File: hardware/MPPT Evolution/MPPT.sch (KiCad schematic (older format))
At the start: 92 parts, among them P1 CONN_01X02, P2 CONN_01X05, P3 CONN_01X02, P4 CONN_01X02, P5 CONN_01X02, P6 CONN_01X02, P7 CONN_01X02, U1 LTC3129, U2 LTC3129, U3 LTC3129, U4 LTC3129, U5 LTC3129, U6 ZXCT1009, U7 ZXCT1009

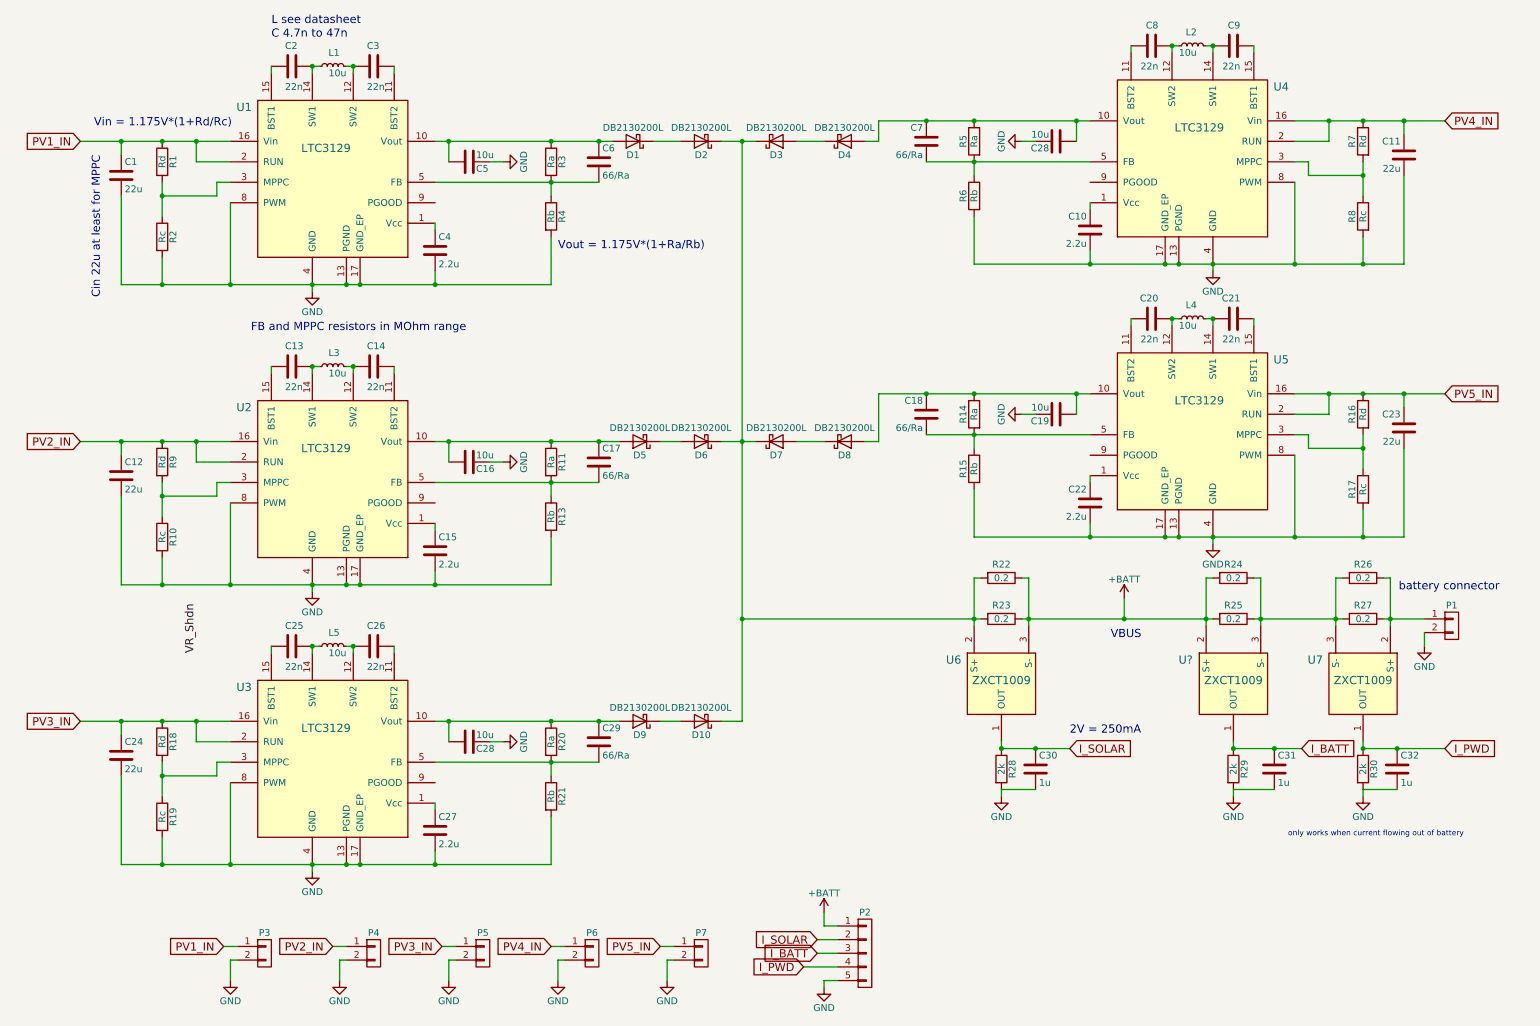
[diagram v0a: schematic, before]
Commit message: Added out pins from panels to MCU
Added out pins from panels to MCU so voltage of each one can be measured
by CPU
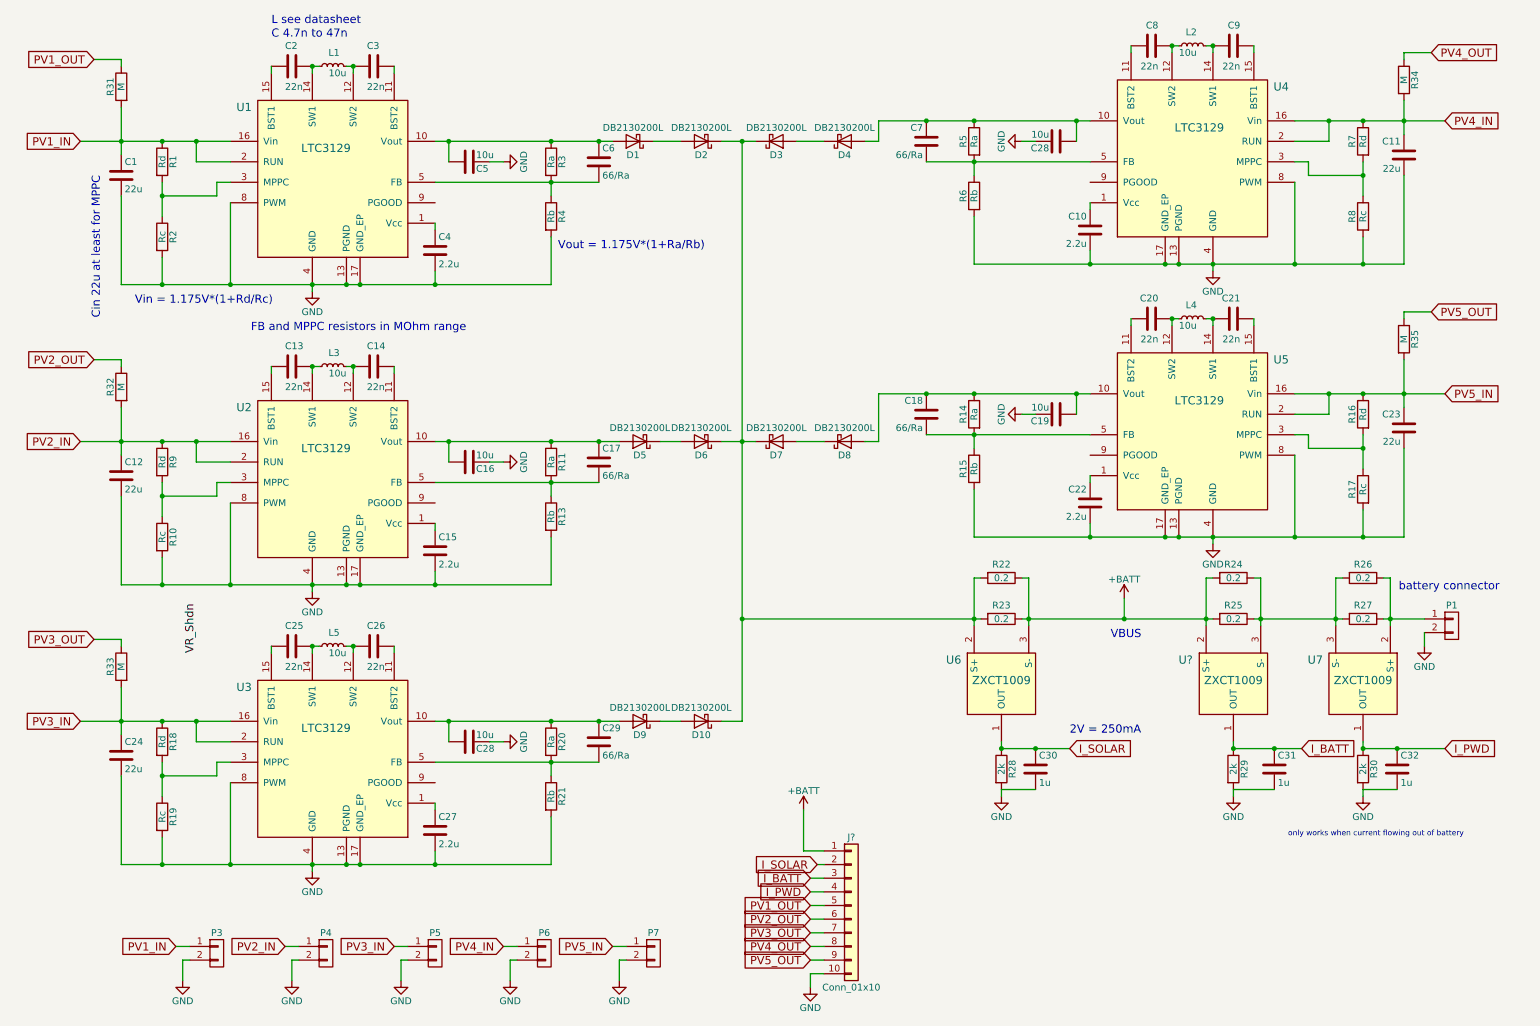
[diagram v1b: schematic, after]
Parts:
- removed P2: CONN_01X05, Pin_Headers:Pin_Header_Straight_1x05, symbol CONN_01X05
- added J?: Conn_01x10, symbol Conn_01x10
- added R31, R32, R33, R34, R35: M, Resistors_SMD:R_0603, symbol R
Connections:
- net +BATT: now also J?.1 (Pin_1)
- net GND: now also J?.10 (Pin_10)
- net I_BATT: now also J?.3 (Pin_3)
- net I_PWD: now also J?.4 (Pin_4)
- net I_SOLAR: now also J?.2 (Pin_2)
- net PV1_IN: now also R31.2
- net PV2_IN: now also R32.2
- net PV3_IN: now also R33.2
- net PV4_IN: now also R34.2
- net PV5_IN: now also R35.2
- new net PV1_OUT: J?.5 (Pin_5), R31.1
- new net PV2_OUT: J?.6 (Pin_6), R32.1
- new net PV3_OUT: J?.7 (Pin_7), R33.1
- new net PV4_OUT: J?.8 (Pin_8), R34.1
- new net PV5_OUT: J?.9 (Pin_9), R35.1
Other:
- moved on the sheet: P3, P4, P5, P6, P7

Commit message: MPPT evolution added missing models, replaced componentes
MPPT evolution added missing models, replaced componentes, routed again.
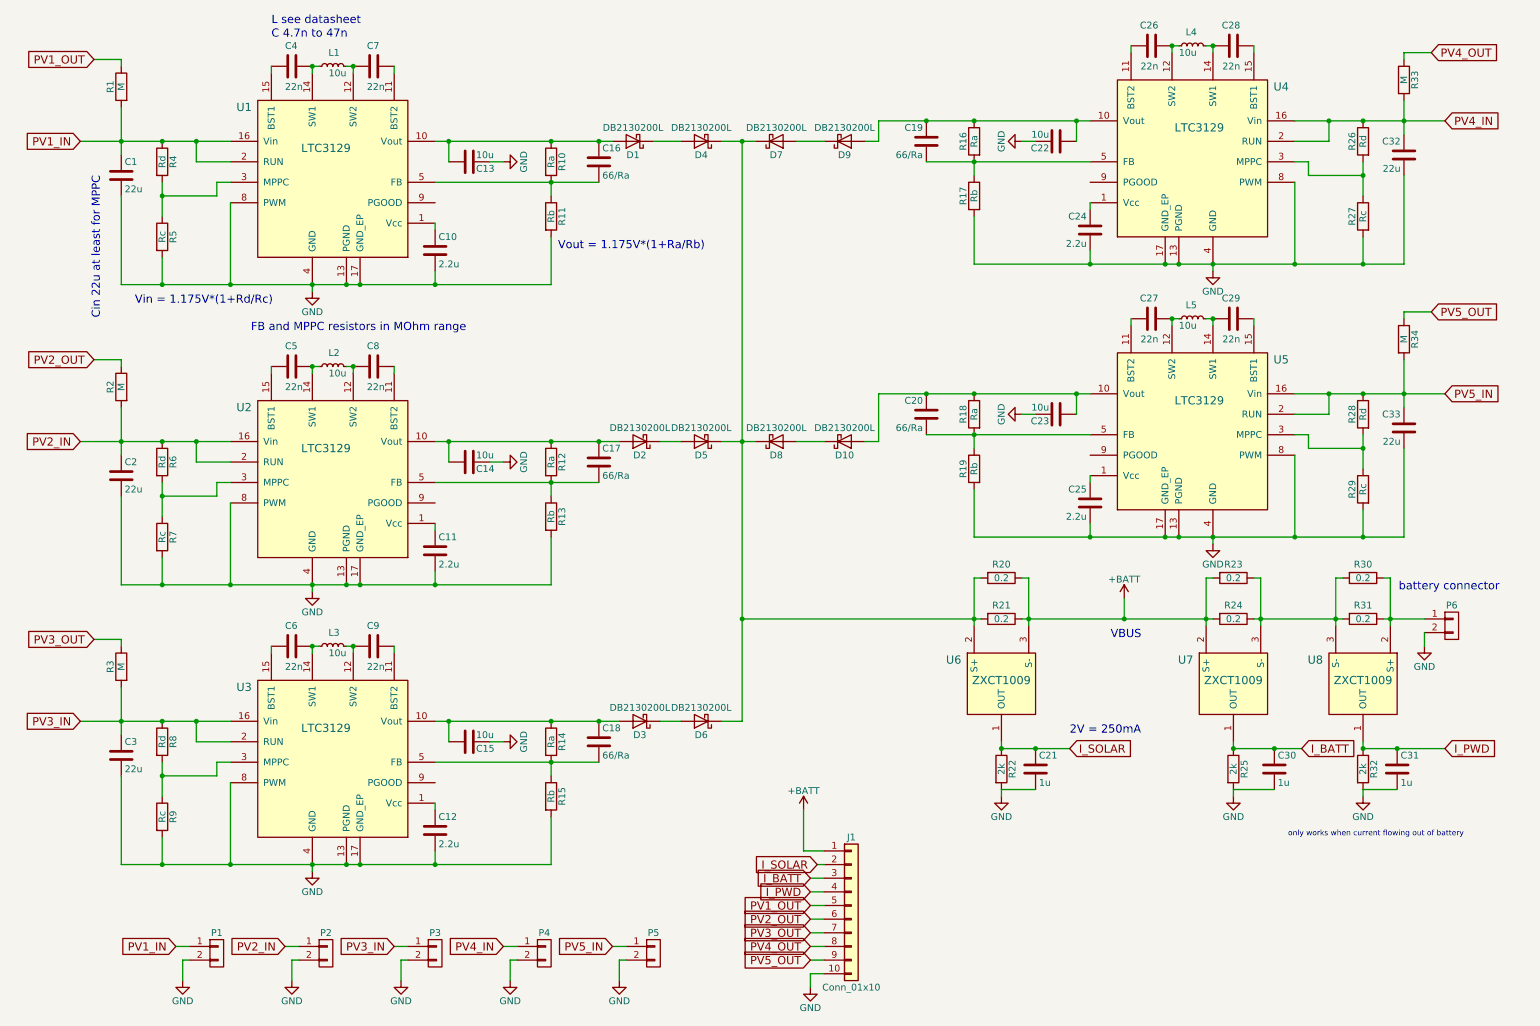
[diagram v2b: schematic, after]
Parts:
- J1: renamed from J?; footprint (none) -> Pin_Headers:Pin_Header_Straight_1x10_Pitch1.27mm
- P1: renamed from P3; footprint Pin_Headers:Pin_Header_Straight_1x02 -> Pin_Headers:Pin_Header_Straight_1x02_Pitch1.27mm
- P2: renamed from P4; footprint Pin_Headers:Pin_Header_Straight_1x02 -> Pin_Headers:Pin_Header_Straight_1x02_Pitch1.27mm
- P3: renamed from P5; footprint Pin_Headers:Pin_Header_Straight_1x02 -> Pin_Headers:Pin_Header_Straight_1x02_Pitch1.27mm
- P4: renamed from P6; footprint Pin_Headers:Pin_Header_Straight_1x02 -> Pin_Headers:Pin_Header_Straight_1x02_Pitch1.27mm
- P5: renamed from P7; footprint Pin_Headers:Pin_Header_Straight_1x02 -> Pin_Headers:Pin_Header_Straight_1x02_Pitch1.27mm
- gave numbers to parts that had none: 1
- renumbered C4 to C10, C15 to C11, C27 to C12, C5 to C13, C16 to C14, C28 to C15, C6 to C16, C29 to C18, C7 to C19, C12 to C2, C18 to C20, C30 to C21, C28 to C22, C19 to C23, C10 to C24, C22 to C25, C8 to C26, C20 to C27, C9 to C28, C21 to C29, C24 to C3, C31 to C30, C32 to C31, C11 to C32, C23 to C33, C2 to C4, C13 to C5, C25 to C6, C3 to C7, C14 to C8, C26 to C9, D8 to D10, D5 to D2, D9 to D3, D2 to D4, D6 to D5, D10 to D6, D3 to D7, D7 to D8, D4 to D9, L3 to L2, L5 to L3, L2 to L4, L4 to L5, P1 to P6, R31 to R1, R3 to R10, R4 to R11, R11 to R12, R20 to R14, R21 to R15, R5 to R16, R6 to R17, R14 to R18, R15 to R19, R32 to R2, R22 to R20, R23 to R21, R28 to R22, R24 to R23, R25 to R24, R29 to R25, R7 to R26, R8 to R27, R16 to R28, R17 to R29, R33 to R3, R26 to R30, R27 to R31, R30 to R32, R34 to R33, R35 to R34, R1 to R4, R2 to R5, R9 to R6, R10 to R7, R18 to R8, R19 to R9, U7 to U8
